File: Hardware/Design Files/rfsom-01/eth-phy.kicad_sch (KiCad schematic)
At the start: 0 parts

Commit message: ddr progress; added more conns;
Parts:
- added U6: KSZ9131RNXI-TR, ICs:MLPQ-48-1EP_7x7mm_P0.5mm, symbol ICs:KSZ9131RNXI-TR
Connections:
- new net ENET0_CLK: U6.46 (XI)
- new net ENET0_MDC: U6.36 (MDC)
- new net ENET0_RSTB: U6.42 (RESET_N)
- new net ENET0_RXCLK: U6.35 (RXC/PHYAD2)
- new net ENET0_RXCTL_R: U6.33 (RX_CTL/CLK125_EN)
- new net ENET0_RXD0_R: U6.32 (RXD0/MODE0)
- new net ENET0_RXD1_R: U6.31 (RXD1/MODE1)
- new net ENET0_RXD2_R: U6.28 (RXD2/MODE2)
- new net ENET0_RXD3_R: U6.27 (RXD3/MODE3)
- new net ENET0_TXCLK_R: U6.24 (TXC)
- new net ENET0_TXCTL_R: U6.25 (TX_CTL)
- new net ENET0_TXD0_R: U6.19 (TXD0)
- new net ENET0_TXD1_R: U6.20 (TXD1)
- new net ENET0_TXD2_R: U6.21 (TXD2)
- new net ENET0_TXD3_R: U6.22 (TXD3)
- new net ETH0_MDIO: U6.37 (MDIO)
- new net SYSCLK: U6.41 (CLK125_NDO/LED_MODE)

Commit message: ps progress; added ftdi; mezz pinout pedinging;
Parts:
- added C? (x12): CL05B104KA5NNNC, Capacitor_SMD:C_0402_1005Metric_Pad0.74x0.62mm_HandSolder, symbol Capacitors:CL05B104KA5NNNC
- added C? (x3): CL31A106KBHNNNE, Capacitor_SMD:C_1206_3216Metric_Pad1.33x1.80mm_HandSolder, symbol Capacitors:CL31A106KBHNNNE
- added C?: CL10B105KA8NNNC, Capacitor_SMD:C_0603_1608Metric_Pad1.08x0.95mm_HandSolder, symbol Capacitors:CL10B105KA8NNNC
- added C?: CL05B103KB5NNNC, Capacitor_SMD:C_0402_1005Metric, symbol Capacitors:CL05B103KB5NNNC
- added C?: CL21B475KAFNNNE, Capacitor_SMD:C_0805_2012Metric_Pad1.18x1.45mm_HandSolder, symbol Capacitors:CL21B475KAFNNNE
- added FB? (x6): MPZ1608S601ATA00, Resistor_SMD:R_0603_1608Metric, symbol Inductors:MPZ1608S601ATA00
- added R? (x6): RC0402FR-0722RL, Resistor_SMD:R_0402_1005Metric, symbol Resistors:RC0402FR-0722RL
- added R? (x6): RC0603FR-071KL, Resistor_SMD:R_0603_1608Metric_Pad0.98x0.95mm_HandSolder, symbol Resistors:RC0603FR-071KL
- added R? (x4): RC0603FR-0710KL, Resistor_SMD:R_0603_1608Metric_Pad0.98x0.95mm_HandSolder, symbol Resistors:RC0603FR-0710KL
- added R?: RC0603FR-076K04L, Resistor_SMD:R_0603_1608Metric, symbol Resistors:RC0603FR-076K04L
- added R?: RES_01, Resistor_SMD:R_0402_1005Metric, symbol Resistors:RC0402FR-074K7L
- added R?: RC0603FR-0749R9L, Resistor_SMD:R_0603_1608Metric, symbol Resistors:RC0603FR-0749R9L
- added Y?: ECS-2033-500-BN, Miscellaneous:ECS-2033-500-BN, symbol Miscellaneous:ECS-2033-500-BN
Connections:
- net ENET0_RSTB: now also C?.2, R?.2
- net ENET0_RXCLK: now also R?.1; no longer U6.35 (RXC/PHYAD2)
- net ENET0_RXCTL_R: now also R?.2
- net ENET0_RXD0_R: now also R?.1, R?.2, R?.2
- net ENET0_RXD1_R: now also R?.1, R?.2, R?.2
- net ENET0_RXD2_R: now also R?.1, R?.2, R?.2
- net ENET0_RXD3_R: now also R?.1, R?.2, R?.2
- net ETH0_MDIO: now also R?.2
- net +ETH_AVDDH: now reaches U6.1 (AVDDH)
- net +ETH_AVDDH: now also U6.12 (AVDDH), U6.4 (AVDDL), U6.9 (AVDDL), C?.1, C?.1, C?.1, FB?.2
- net ETH_TXRXD+: now reaches U6.10 (TXRXP_D)
- net ETH_TXRXD-: now reaches U6.11 (TXRXM_D)
- net ETH_LED1: now reaches U6.15 (LED2/PHYAD1)
- net ETH_LED1: now also R?.1
- net +ETH_DVDDH: now reaches U6.16 (DVDDH)
- net +ETH_DVDDH: now also U6.34 (DVDDH), U6.40 (DVDDH), FB?.2, FB?.2, R?.2
- net ETH_LED0: now reaches U6.17 (LED1/PME_N1//PHYAD0)
- net +ETH_DVDDL: now reaches U6.18 (DVDDL)
- net +ETH_DVDDL: now also U6.23 (DVDDL), U6.26 (DVDDL), U6.30 (DVDDL), U6.39 (DVDDL), C?.1, C?.1, C?.1, C?.1, C?.1, C?.1, FB?.2
- net ETH_TXRXA+: now reaches U6.2 (TXRXP_A)
- net GND: now reaches U6.29 (VSS)
- net GND: now also U6.45 (XO), U6.49 (EP), C?.1, C?.2, C?.2, C?.2, C?.2, C?.2, C?.2, C?.2, C?.2, C?.2, C?.2, C?.2, C?.2, C?.2, C?.2, C?.2, C?.2, C?.2, R?.2, R?.2, R?.2, R?.2, R?.2, Y?.2 (GND)
- net ETH_TXRXA-: now reaches U6.3 (TXRXM_A)
- net at U6.44 (AVDDL_PLL): now also C?.1, C?.1, C?.1, FB?.1
- net at U6.48 (ISET): now also R?.1
- net ETH_TXRXB+: now reaches U6.5 (TXRXP_B)
- net ETH_TXRXB-: now reaches U6.6 (TXRXM_B)
- net ETH_TXRXC+: now reaches U6.7 (TXRXP_C)
- net ETH_TXRXC-: now reaches U6.8 (TXRXM_C)
- net ENET0_CLK: no longer names the net of U6.46 (XI)
- net ENET0_CLK: now also R?.2
- net ENET0_TXCLK_R renamed ENET0_TXCLK
- net ENET0_TXCTL_R renamed ENET0_TXCTL
- net ENET0_TXD0_R renamed ENET0_TXD0
- net ENET0_TXD1_R renamed ENET0_TXD1
- net ENET0_TXD2_R renamed ENET0_TXD2
- net ENET0_TXD3_R renamed ENET0_TXD3
- new net: R?.1, Y?.3 (OUT)
- new net +ETH_AVDDL: C?.1, C?.1, C?.1, C?.1, FB?.1
- new net +VCC_1V2: FB?.1, FB?.2, FB?.2
- new net +VCC_1V8: FB?.1, R?.1, R?.1, R?.1, R?.1, R?.1
- new net +VCC_3V3: C?.1, FB?.1, FB?.1, R?.1, Y?.1 (EN), Y?.4 (VDD)
- new net ENET0_RXCLK_R: R?.2, U6.35 (RXC/PHYAD2)
- new net ENET0_RXCTL: R?.1
- new net ENET0_RXD0: R?.1
- new net ENET0_RXD1: R?.1
- new net ENET0_RXD2: R?.1
- new net ENET0_RXD3: R?.1
- no-connect marks 0 -> 3
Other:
- moved on the sheet: U6

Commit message: some ddr routing progress; layerstack per pcbway standard options, review reqd; commit prior to ddr split;
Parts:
- C16, C17, C20, C21, C22, C23, C24, C27, C30, C31, C32, C7: renamed from C?; footprint Capacitor_SMD:C_0402_1005Metric_Pad0.74x0.62mm_HandSolder -> Capacitor_SMD:C_0402_1005Metric
- C18: renamed from C?; footprint Capacitor_SMD:C_0603_1608Metric_Pad1.08x0.95mm_HandSolder -> Capacitor_SMD:C_0603_1608Metric
- C19, C26, C29: renamed from C?; footprint Capacitor_SMD:C_1206_3216Metric_Pad1.33x1.80mm_HandSolder -> Capacitor_SMD:C_1206_3216Metric
- C25: renamed from C?; footprint Capacitor_SMD:C_0805_2012Metric_Pad1.18x1.45mm_HandSolder -> Capacitor_SMD:C_0805_2012Metric
- R13, R14, R15, R16, R17, R18, R19, R20, R31, R33: renamed from R?; footprint Resistor_SMD:R_0603_1608Metric_Pad0.98x0.95mm_HandSolder -> Resistor_SMD:R_0603_1608Metric
- gave numbers to parts that had none: 17
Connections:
- net ETH_LED0 is gone; now on net ETH_LED1: U6.17 (LED1/PME_N1//PHYAD0)
- net ETH_LED1: no longer R33.1, U6.15 (LED2/PHYAD1)
- net +ETH_1V2: now reaches C25.1, C27.1, C28.1, FB6.1, U6.44 (AVDDL_PLL)
- net ENET0_RSTB renamed ~{ENET0_RST}
- new net ETH_LED2: R33.1, U6.15 (LED2/PHYAD1)
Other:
- moved on the sheet: C16, C17, C19, C20, C21, C22, C23, C24, C26, C29, C30, C31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

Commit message: added starage, usb sch; more design progress in sch;
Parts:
- removed C7: CL05B104KA5NNNC, Capacitor_SMD:C_0402_1005Metric, symbol Capacitors:CL05B104KA5NNNC
- removed Y1: ECS-2033-500-BN, Miscellaneous:ECS-2033-500-BN, symbol Miscellaneous:ECS-2033-500-BN
- added C185: CL05B104KA5NNNC, Capacitor_SMD:C_0402_1005Metric, symbol Capacitors:CL05B104KA5NNNC
- added Y3: ECS-2033-250-BN, Miscellaneous:ECS-2033, symbol Miscellaneous:ECS-2033-250-BN
- R22, R23, R27, R28, R29, R30: footprint Resistor_SMD:R_0402_1005Metric -> Resistor_SMD:R_0603_1608Metric; symbol Resistors:RC0402FR-0722RL -> Resistors:RC0603FR-0749R9L; Resistance 22R -> 49.9R
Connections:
- net +VCC_3V3: now also C185.1, Y3.1 (EN), Y3.4 (VDD)
- net GND: now also C185.2, Y3.2 (GND)
- net at R21.1: now also Y3.3 (OUT)
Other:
- moved on the sheet: R32

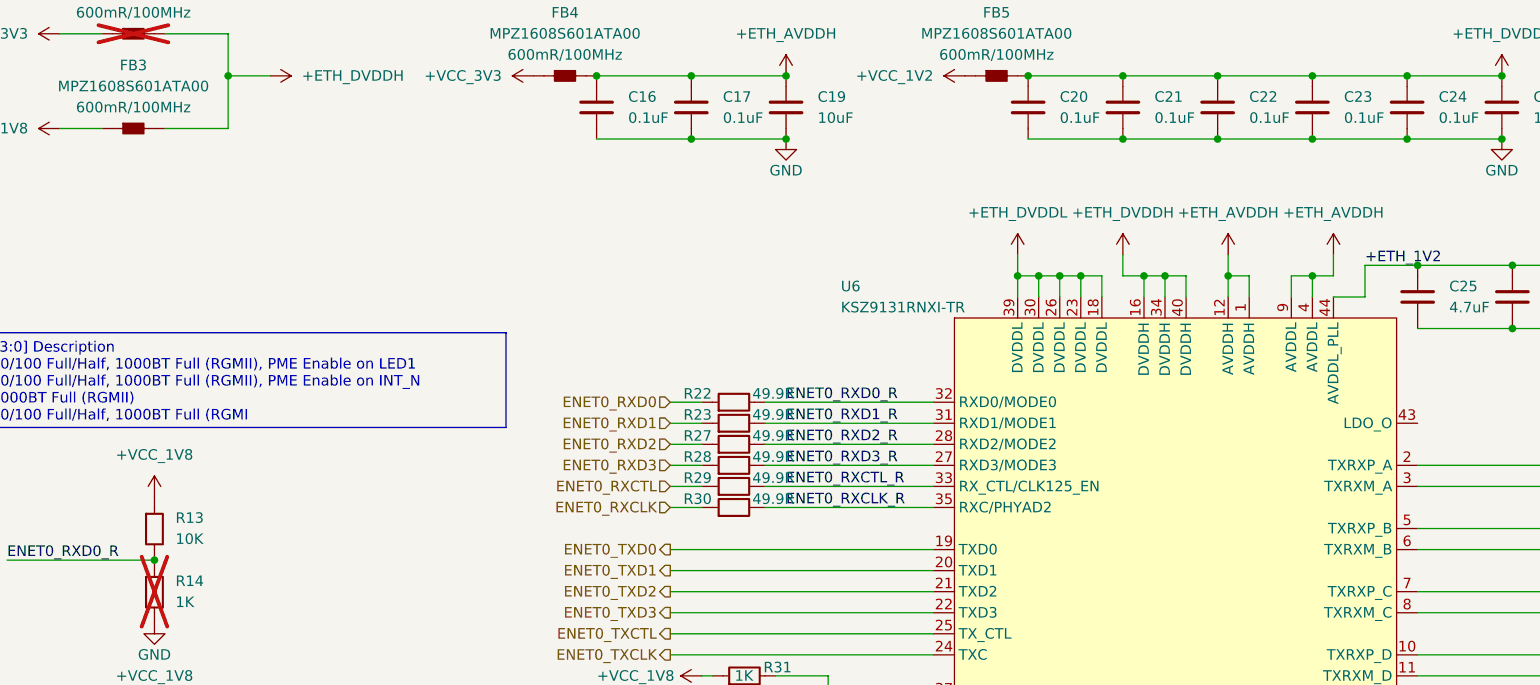
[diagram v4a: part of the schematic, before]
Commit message: routing changes; added mezzanine; added pl ram;
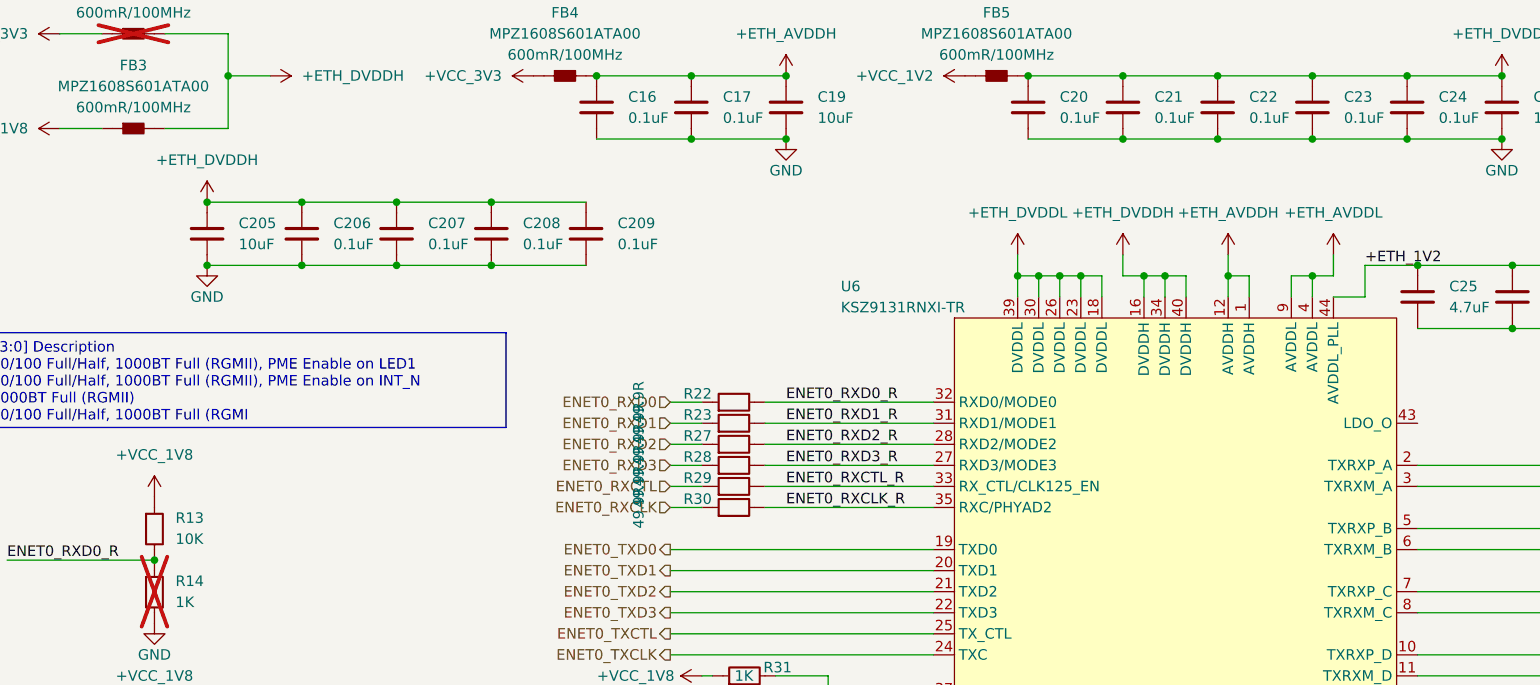
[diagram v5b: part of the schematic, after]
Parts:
- added C205: CL31A106KBHNNNE, Capacitor_SMD:C_1206_3216Metric, symbol Capacitors:CL31A106KBHNNNE
- added C206, C207, C208, C209: CL05B104KA5NNNC, Capacitor_SMD:C_0402_1005Metric, symbol Capacitors:CL05B104KA5NNNC
- R22, R23, R27, R28, R29, R30: footprint Resistor_SMD:R_0603_1608Metric -> Resistor_SMD:R_0402_1005Metric_Pad0.72x0.64mm_HandSolder; symbol Resistors:RC0603FR-0749R9L -> Resistors:RC0402FR-0749R9L
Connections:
- net +ETH_AVDDH: no longer U6.4 (AVDDL), U6.9 (AVDDL)
- net +ETH_AVDDL: now also U6.4 (AVDDL), U6.9 (AVDDL)
- net +ETH_DVDDH: now also C205.1, C206.1, C207.1, C208.1, C209.1
- net GND: now also C205.2, C206.2, C207.2, C208.2, C209.2

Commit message: updated sch pdf; routign progress;
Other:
- moved on the sheet: R22, R23, R27, R28, R29, R30

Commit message: replaced pmic;
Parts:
- R22, R23, R27, R28, R29, R30: footprint Resistor_SMD:R_0402_1005Metric_Pad0.72x0.64mm_HandSolder -> Resistor_SMD:R_0402_1005Metric
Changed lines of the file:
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@@
 			)
 		)
-		(property "Footprint" "Resistor_SMD:R_0402_1005Metric_Pad0.72x0.64mm_HandSolder"
+		(property "Footprint" "Resistor_SMD:R_0402_1005Metric"
 			(at 101.6 74.93 0)
 			(effects
@@
 			)
 		)
-		(property "Footprint" "Resistor_SMD:R_0402_1005Metric_Pad0.72x0.64mm_HandSolder"
+		(property "Footprint" "Resistor_SMD:R_0402_1005Metric"
 			(at 101.6 80.01 0)
 			(effects
@@
 			)
 		)
-		(property "Footprint" "Resistor_SMD:R_0402_1005Metric_Pad0.72x0.64mm_HandSolder"
+		(property "Footprint" "Resistor_SMD:R_0402_1005Metric"
 			(at 101.6 67.31 0)
 			(effects
@@
 			)
 		)
-		(property "Footprint" "Resistor_SMD:R_0402_1005Metric_Pad0.72x0.64mm_HandSolder"
+		(property "Footprint" "Resistor_SMD:R_0402_1005Metric"
 			(at 101.6 77.47 0)
 			(effects
@@
 			)
 		)
-		(property "Footprint" "Resistor_SMD:R_0402_1005Metric_Pad0.72x0.64mm_HandSolder"
+		(property "Footprint" "Resistor_SMD:R_0402_1005Metric"
 			(at 101.6 69.85 0)
 			(effects
@@
 			)
 		)
-		(property "Footprint" "Resistor_SMD:R_0402_1005Metric_Pad0.72x0.64mm_HandSolder"
+		(property "Footprint" "Resistor_SMD:R_0402_1005Metric"
 			(at 101.6 72.39 0)
 			(effects
